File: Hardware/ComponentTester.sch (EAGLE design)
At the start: 0 parts

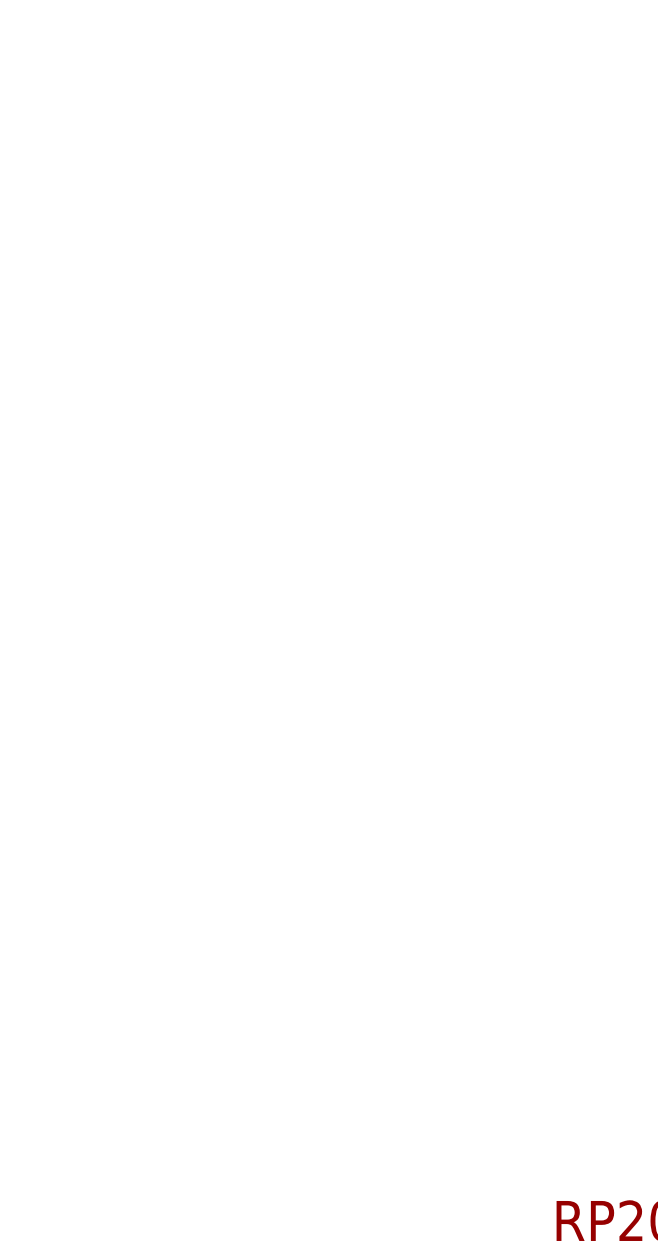
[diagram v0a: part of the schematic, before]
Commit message: Add RP2040
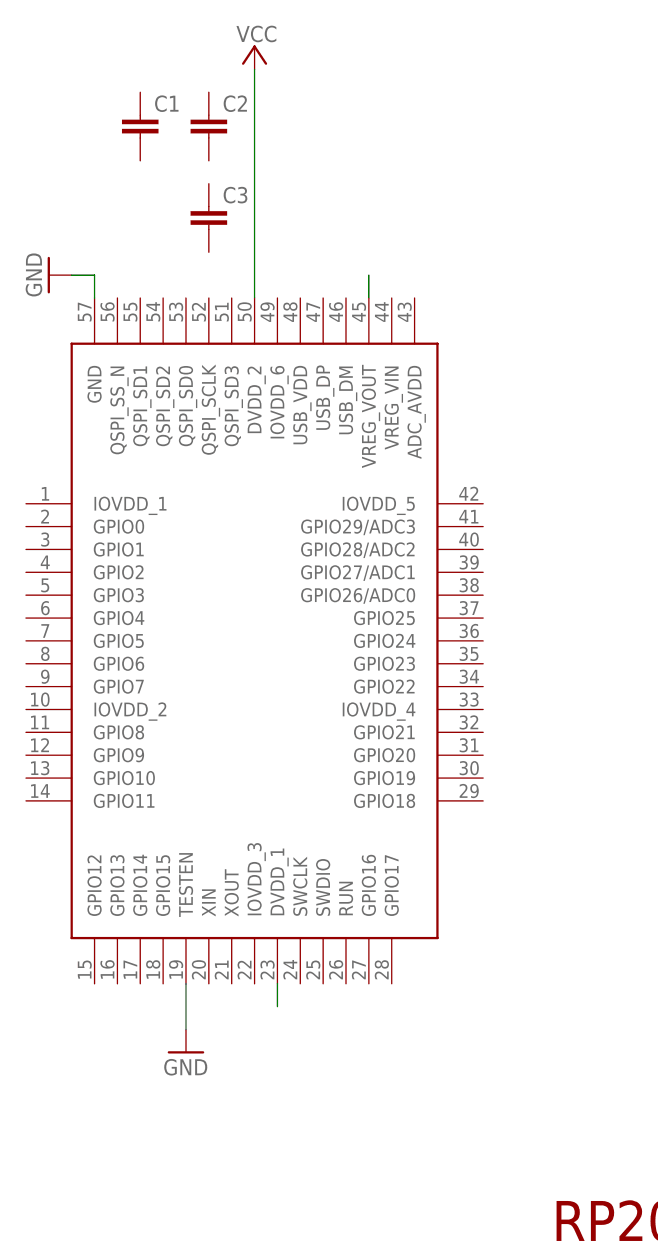
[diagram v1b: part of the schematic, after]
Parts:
- added C1, C2, C3: (no value), rcl:C-EUC0603
- added IC1: RP2040TR13, RP2040TR13:RP2040TR13
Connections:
- new net GND: IC1.GND, IC1.TESTEN
- new net N$2: IC1.VREG_VOUT
- new net N$4: IC1.DVDD_1
- new net VCC: IC1.DVDD_2
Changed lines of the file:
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@@
 <parts>
 <part name="FRAME1" library="frames" library_urn="urn:adsk.eagle:library:229" deviceset="A4L-LOC" device=""/>
+<part name="IC1" library="RP2040TR13" deviceset="RP2040TR13" device=""/>
+<part name="GND1" library="supply1" library_urn="urn:adsk.eagle:library:371" deviceset="GND" device=""/>
+<part name="GND2" library="supply1" library_urn="urn:adsk.eagle:library:371" deviceset="GND" device=""/>
+<part name="C2" library="rcl" library_urn="urn:adsk.eagle:library:334" deviceset="C-EU" device="C0603" package3d_urn="urn:adsk.eagle:package:23616/2"/>
+<part name="C1" library="rcl" library_urn="urn:adsk.eagle:library:334" deviceset="C-EU" device="C0603" package3d_urn="urn:adsk.eagle:package:23616/2"/>
+<part name="C3" library="rcl" library_urn="urn:adsk.eagle:library:334" deviceset="C-EU" device="C0603" package3d_urn="urn:adsk.eagle:package:23616/2"/>
+<part name="P+1" library="supply1" library_urn="urn:adsk.eagle:library:371" deviceset="VCC" device=""/>
 </parts>
 <sheets>
@@
 <attribute name="SHEET" x="231.775" y="6.35" size="2.54" layer="94"/>
 </instance>
+<instance part="IC1" gate="G$1" x="106.68" y="101.6" smashed="yes"/>
+<instance part="GND1" gate="1" x="109.22" y="127" smashed="yes" rot="R270">
+<attribute name="VALUE" x="106.68" y="129.54" size="1.778" layer="96" rot="R270"/>
+</instance>
+<instance part="GND2" gate="1" x="124.46" y="40.64" smashed="yes">
+<attribute name="VALUE" x="121.92" y="38.1" size="1.778" layer="96"/>
+</instance>
+<instance part="C2" gate="G$1" x="127" y="144.78" smashed="yes">
+<attribute name="NAME" x="128.524" y="145.161" size="1.778" layer="95"/>
+<attribute name="VALUE" x="128.524" y="140.081" size="1.778" layer="96"/>
+</instance>
+<instance part="C1" gate="G$1" x="119.38" y="144.78" smashed="yes">
+<attribute name="NAME" x="120.904" y="145.161" size="1.778" layer="95"/>
+<attribute name="VALUE" x="120.904" y="140.081" size="1.778" layer="96"/>
+</instance>
+<instance part="C3" gate="G$1" x="127" y="134.62" smashed="yes">
+<attribute name="NAME" x="128.524" y="135.001" size="1.778" layer="95"/>
+<attribute name="VALUE" x="128.524" y="129.921" size="1.778" layer="96"/>
+</instance>
+<instance part="P+1" gate="VCC" x="132.08" y="152.4" smashed="yes">
+<attribute name="VALUE" x="134.62" y="154.686" size="1.778" layer="96" rot="R180"/>
+</instance>
 </instances>
 <busses>
 </busses>
 <nets>
+<net name="GND" class="0">
+<segment>
+<pinref part="IC1" gate="G$1" pin="GND"/>
+<wire x1="114.3" y1="124.46" x2="114.3" y2="127" width="0.1524" layer="91"/>
+<pinref part="GND1" gate="1" pin="GND"/>
+<wire x1="114.3" y1="127" x2="111.76" y2="127" width="0.1524" layer="91"/>
+</segment>
+<segment>
+<pinref part="GND2" gate="1" pin="GND"/>
+<pinref part="IC1" gate="G$1" pin="TESTEN"/>
+<wire x1="124.46" y1="43.18" x2="124.46" y2="48.26" width="0.1524" layer="91"/>
+</segment>
+</net>
+<net name="N$2" class="0">
+<segment>
+<pinref part="IC1" gate="G$1" pin="VREG_VOUT"/>
+<wire x1="144.78" y1="124.46" x2="144.78" y2="127" width="0.1524" layer="91"/>
+</segment>
+</net>
+<net name="N$4" class="0">
+<segment>
+<pinref part="IC1" gate="G$1" pin="DVDD_1"/>
+<wire x1="134.62" y1="48.26" x2="134.62" y2="45.72" width="0.1524" layer="91"/>
+</segment>
+</net>
+<net name="VCC" class="0">
+<segment>
+<pinref part="IC1" gate="G$1" pin="DVDD_2"/>
+<wire x1="132.08" y1="124.46" x2="132.08" y2="149.86" width="0.1524" layer="91"/>
+<pinref part="P+1" gate="VCC" pin="VCC"/>
+</segment>
+</net>
 </nets>
 </sheet>
@@
 will not be understood (or retained) with this version.
 </note>
+<note version="8.3" severity="warning">
+Since Version 8.3, EAGLE supports the association of 3D packages
+with devices in libraries, schematics, and board files. Those 3D
+packages will not be understood (or retained) with this version.
+</note>
+<note version="8.4" severity="warning">
+Since Version 8.4, EAGLE supports properties for SPICE simulation.
+Probes in schematics and SPICE mapping objects found in parts and library devices
+will not be understood with this version. Update EAGLE to the latest version
+for full support of SPICE simulation.
+</note>
 </compatibility>

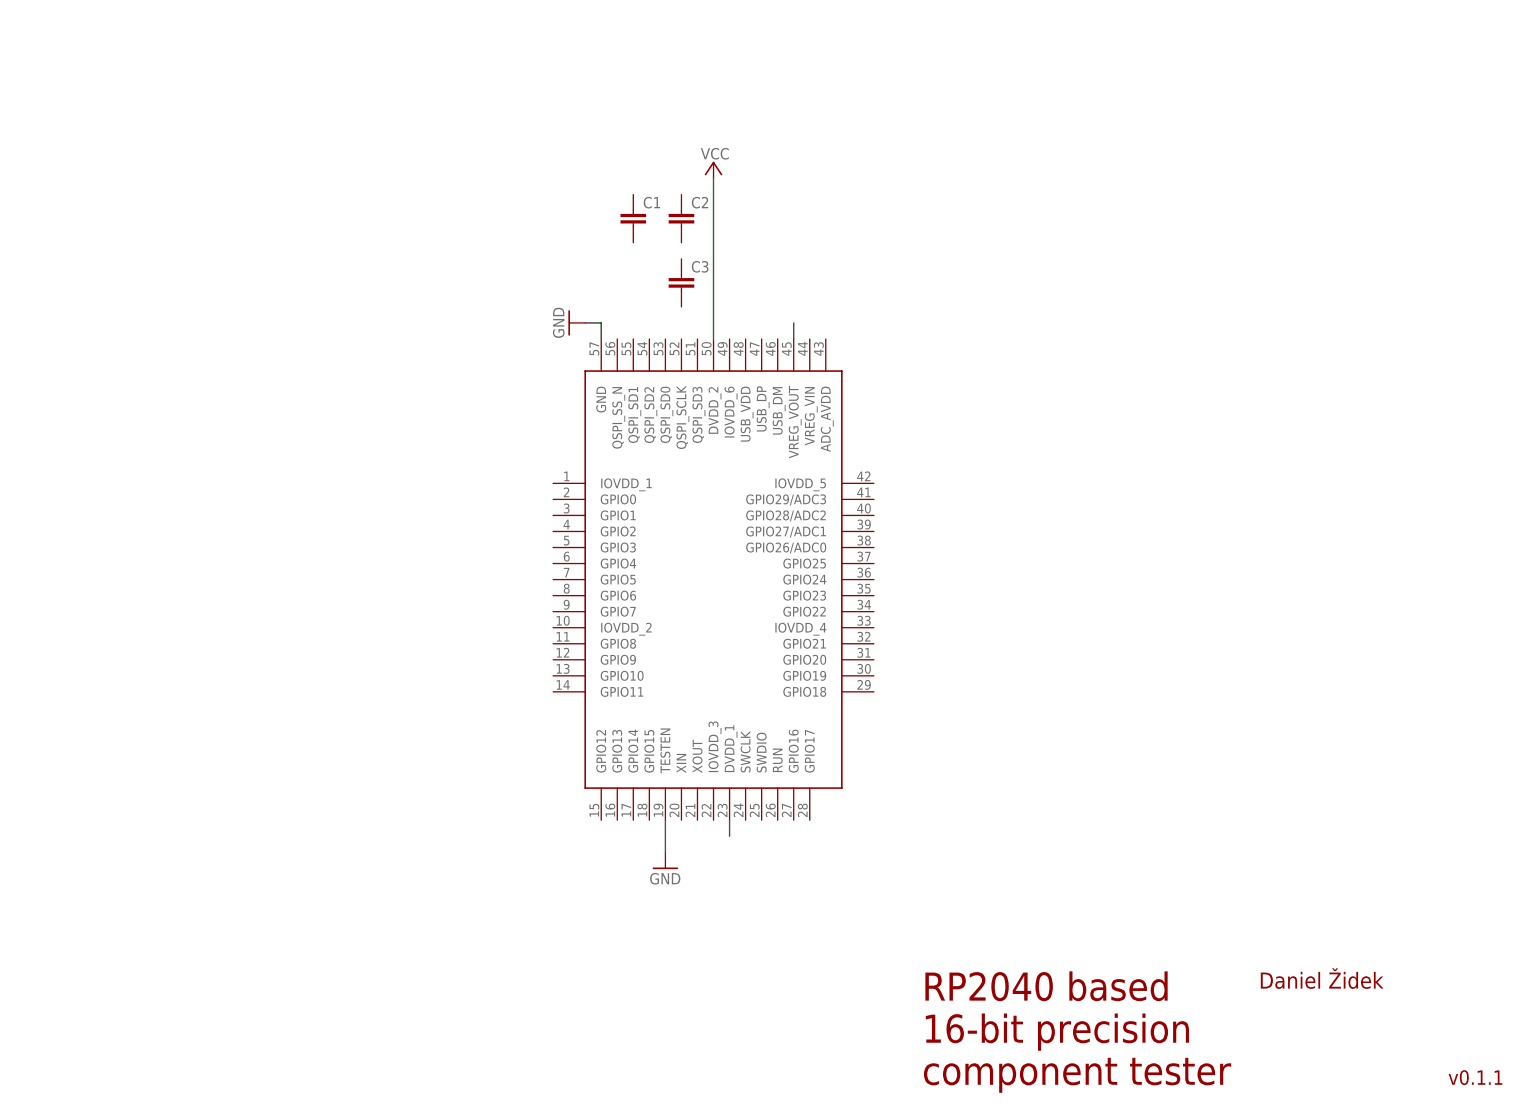
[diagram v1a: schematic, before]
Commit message: Add array of decoupling capacitors
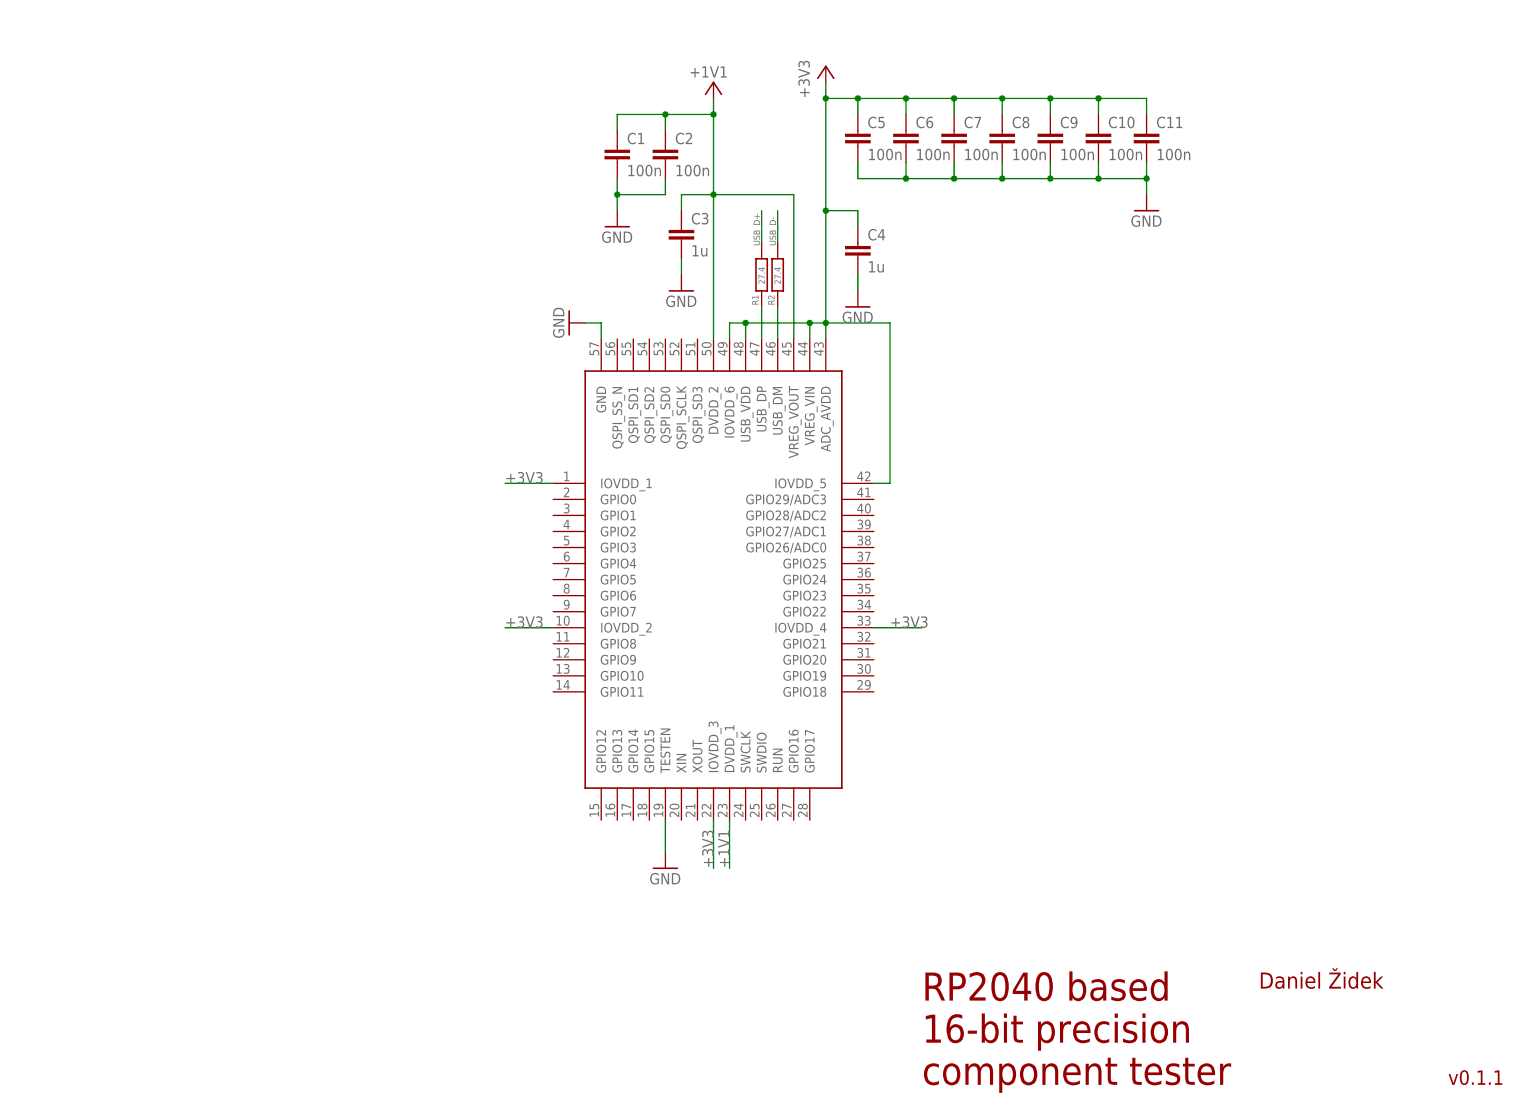
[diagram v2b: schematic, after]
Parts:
- added C10, C11, C5, C6, C7, C8, C9: 100n, rcl:C-EUC0603
- added C4: 1u, rcl:C-EUC0603
- added R1, R2: 27.4, rcl:R-EU_R0805
- C1, C2: value (none) -> 100n
- C3: value (none) -> 1u
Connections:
- removed net N$4: IC1.DVDD_1
- removed net VCC: IC1.DVDD_2
- new net +1V1: C1.1, C2.1, C3.1, IC1.DVDD_1, IC1.DVDD_2, IC1.VREG_VOUT
- new net +3V3: C10.1, C11.1, C4.1, C5.1, C6.1, C7.1, C8.1, C9.1, IC1.ADC_AVDD, IC1.IOVDD_1, IC1.IOVDD_2, IC1.IOVDD_3, IC1.IOVDD_4, IC1.IOVDD_5, IC1.IOVDD_6, IC1.USB_VDD, IC1.VREG_VIN
- new net N$1: IC1.USB_DP, R1.1
- new net USB_D+: R1.2
- new net USB_D-: R2.2
- net GND: now also C1.2, C10.2, C11.2, C2.2, C3.2, C4.2, C5.2, C6.2, C7.2, C8.2, C9.2
- net N$2: now also IC1.USB_DM, R2.1; no longer IC1.VREG_VOUT
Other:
- moved on the sheet: C1, C2, C3

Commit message: Add LDO
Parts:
- added C12, C13: 10u, rcl:C-EUC0603
- added IC2: NCP1117ST33T3G, NCP1117ST33T3G:NCP1117ST33T3G
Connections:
- new net GPIO0: IC1.GPIO0
- new net GPIO1: IC1.GPIO1
- new net GPIO10: IC1.GPIO10
- new net GPIO11: IC1.GPIO11
- new net GPIO12: IC1.GPIO12
- new net GPIO13: IC1.GPIO13
- new net GPIO14: IC1.GPIO14
- new net GPIO15: IC1.GPIO15
- new net GPIO16: IC1.GPIO16
- new net GPIO17: IC1.GPIO17
- new net GPIO18: IC1.GPIO18
- new net GPIO19: IC1.GPIO19
- new net GPIO2: IC1.GPIO2
- new net GPIO20: IC1.GPIO20
- new net GPIO21: IC1.GPIO21
- new net GPIO22: IC1.GPIO22
- new net GPIO23: IC1.GPIO23
- new net GPIO24: IC1.GPIO24
- new net GPIO25: IC1.GPIO25
- new net GPIO26_ADC0: IC1.GPIO26/ADC0
- new net GPIO27_ADC1: IC1.GPIO27/ADC1
- new net GPIO28_ADC2: IC1.GPIO28/ADC2
- new net GPIO29_ADC3: IC1.GPIO29/ADC3
- new net GPIO3: IC1.GPIO3
- new net GPIO4: IC1.GPIO4
- new net GPIO5: IC1.GPIO5
- new net GPIO6: IC1.GPIO6
- new net GPIO7: IC1.GPIO7
- new net GPIO8: IC1.GPIO8
- new net GPIO9: IC1.GPIO9
- new net N$3: C13.1, IC2.INPUT
- new net QSPI_SCLK: IC1.QSPI_SCLK
- new net QSPI_SD0: IC1.QSPI_SD0
- new net QSPI_SD1: IC1.QSPI_SD1
- new net QSPI_SD2: IC1.QSPI_SD2
- new net QSPI_SD3: IC1.QSPI_SD3
- new net QSPI_SS: IC1.QSPI_SS_N
- new net RUN: IC1.RUN
- new net SWCLK: IC1.SWCLK
- new net SWD: IC1.SWDIO
- new net XIN: IC1.XIN
- new net XOUT: IC1.XOUT
- net +3V3: now also C12.1, IC2.OUTPUT_1
- net GND: now also C12.2, C13.2, IC2.ADJUST/GROUND
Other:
- moved on the sheet: C1, C10, C11, C2, C3, C5, C6, C7, C8, C9

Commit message: Add power supply circuit and USB-C 2.0 connector
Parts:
- removed C12, C13: 10u, rcl:C-EUC0603
- removed IC2: NCP1117ST33T3G, NCP1117ST33T3G:NCP1117ST33T3G
- added C25, C26: 10u, rcl:C-EUC0603
- added IC4: NCP1117ST33T3G, NCP1117ST33T3G:NCP1117ST33T3G
- added J1: 629722000214, Eagle_WR-USB (rev22c):629722000214
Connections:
- removed net N$3: C13.1, IC2.INPUT
- new net N$6: C26.1, IC4.INPUT
- net +3V3: now also C25.1, IC4.OUTPUT_1; no longer C12.1, IC2.OUTPUT_1
- net GND: now also C25.2, C26.2, IC4.ADJUST/GROUND; no longer C12.2, C13.2, IC2.ADJUST/GROUND

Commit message: Clear schematics
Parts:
- removed C1, C10, C11, C2, C5, C6, C7, C8, C9: 100n, rcl:C-EUC0603
- removed C25, C26: 10u, rcl:C-EUC0603
- removed C3, C4: 1u, rcl:C-EUC0603
- removed IC1: RP2040TR13, RP2040TR13:RP2040TR13
- removed IC4: NCP1117ST33T3G, NCP1117ST33T3G:NCP1117ST33T3G
- removed J1: 629722000214, Eagle_WR-USB (rev22c):629722000214
- removed R1, R2: 27.4, rcl:R-EU_R0805
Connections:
- removed net +1V1: C1.1, C2.1, C3.1, IC1.DVDD_1, IC1.DVDD_2, IC1.VREG_VOUT
- removed net +3V3: C10.1, C11.1, C25.1, C4.1, C5.1, C6.1, C7.1, C8.1, C9.1, IC1.ADC_AVDD, IC1.IOVDD_1, IC1.IOVDD_2, IC1.IOVDD_3, IC1.IOVDD_4, IC1.IOVDD_5, IC1.IOVDD_6, IC1.USB_VDD, IC1.VREG_VIN, IC4.OUTPUT_1
- removed net GND: C1.2, C10.2, C11.2, C2.2, C25.2, C26.2, C3.2, C4.2, C5.2, C6.2, C7.2, C8.2, C9.2, IC1.GND, IC1.TESTEN, IC4.ADJUST/GROUND
- removed net GPIO0: IC1.GPIO0
- removed net GPIO1: IC1.GPIO1
- removed net GPIO10: IC1.GPIO10
- removed net GPIO11: IC1.GPIO11
- removed net GPIO12: IC1.GPIO12
- removed net GPIO13: IC1.GPIO13
- removed net GPIO14: IC1.GPIO14
- removed net GPIO15: IC1.GPIO15
- removed net GPIO16: IC1.GPIO16
- removed net GPIO17: IC1.GPIO17
- removed net GPIO18: IC1.GPIO18
- removed net GPIO19: IC1.GPIO19
- removed net GPIO2: IC1.GPIO2
- removed net GPIO20: IC1.GPIO20
- removed net GPIO21: IC1.GPIO21
- removed net GPIO22: IC1.GPIO22
- removed net GPIO23: IC1.GPIO23
- removed net GPIO24: IC1.GPIO24
- removed net GPIO25: IC1.GPIO25
- removed net GPIO26_ADC0: IC1.GPIO26/ADC0
- removed net GPIO27_ADC1: IC1.GPIO27/ADC1
- removed net GPIO28_ADC2: IC1.GPIO28/ADC2
- removed net GPIO29_ADC3: IC1.GPIO29/ADC3
- removed net GPIO3: IC1.GPIO3
- removed net GPIO4: IC1.GPIO4
- removed net GPIO5: IC1.GPIO5
- removed net GPIO6: IC1.GPIO6
- removed net GPIO7: IC1.GPIO7
- removed net GPIO8: IC1.GPIO8
- removed net GPIO9: IC1.GPIO9
- removed net N$1: IC1.USB_DP, R1.1
- removed net N$2: IC1.USB_DM, R2.1
- removed net N$6: C26.1, IC4.INPUT
- removed net QSPI_SCLK: IC1.QSPI_SCLK
- removed net QSPI_SD0: IC1.QSPI_SD0
- removed net QSPI_SD1: IC1.QSPI_SD1
- removed net QSPI_SD2: IC1.QSPI_SD2
- removed net QSPI_SD3: IC1.QSPI_SD3
- removed net QSPI_SS: IC1.QSPI_SS_N
- removed net RUN: IC1.RUN
- removed net SWCLK: IC1.SWCLK
- removed net SWD: IC1.SWDIO
- removed net USB_D+: R1.2
- removed net USB_D-: R2.2
- removed net XIN: IC1.XIN
- removed net XOUT: IC1.XOUT
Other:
- note added: "ComponentTester dev-v0.1.1"
- note removed: "RP2040 based 16-bit precision component tester"
